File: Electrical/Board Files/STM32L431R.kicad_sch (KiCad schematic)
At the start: 11 parts, among them U3 STM32L431RCTx

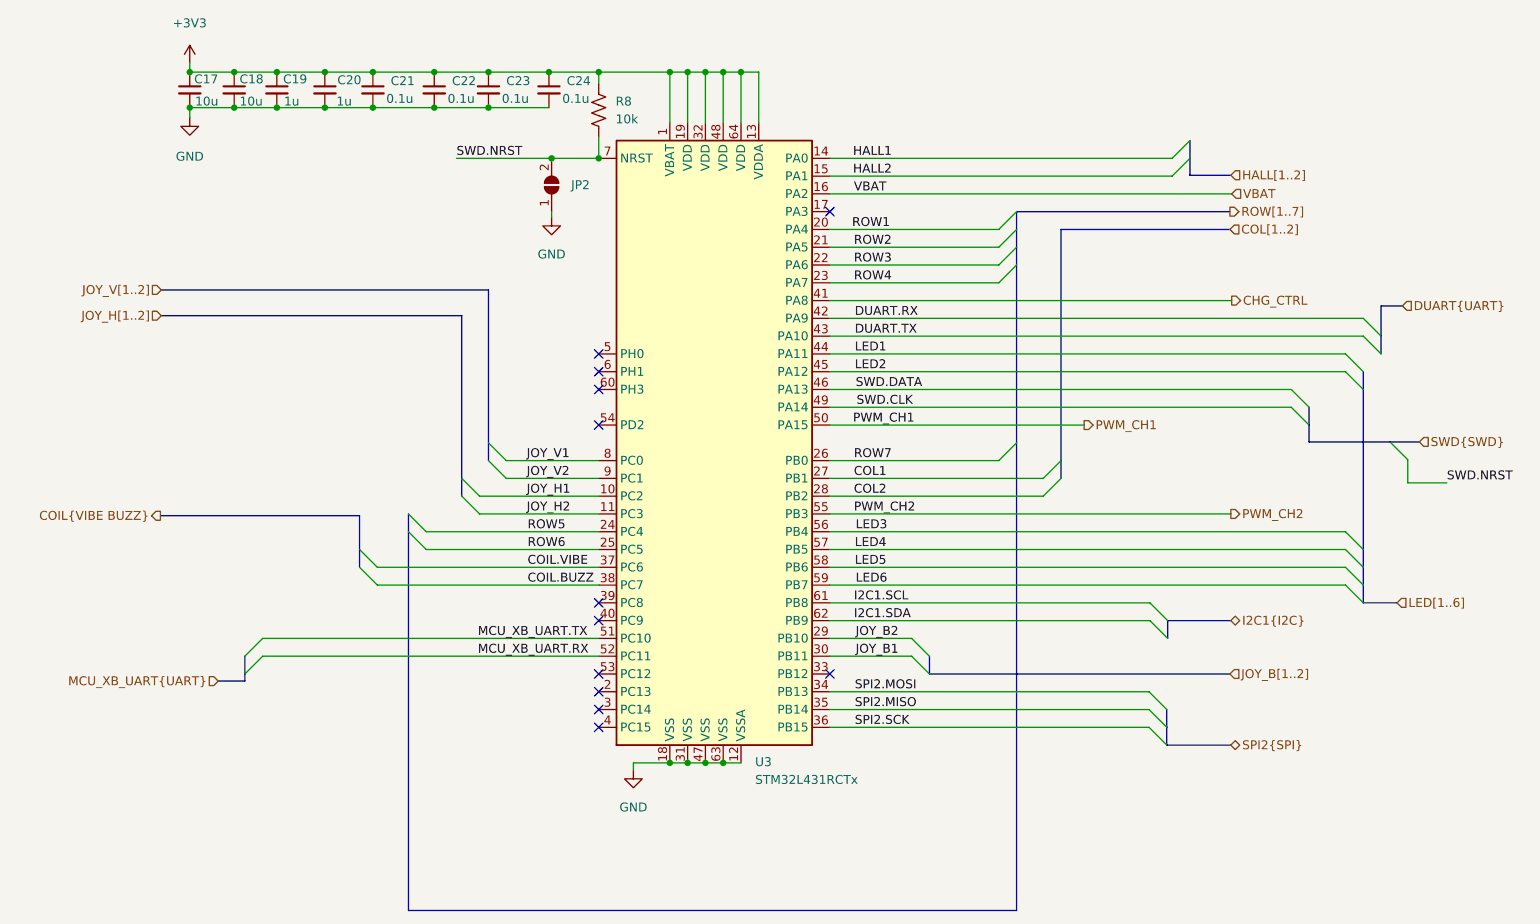
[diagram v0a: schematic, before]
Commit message: Fixing USB pins and added SPI_CS
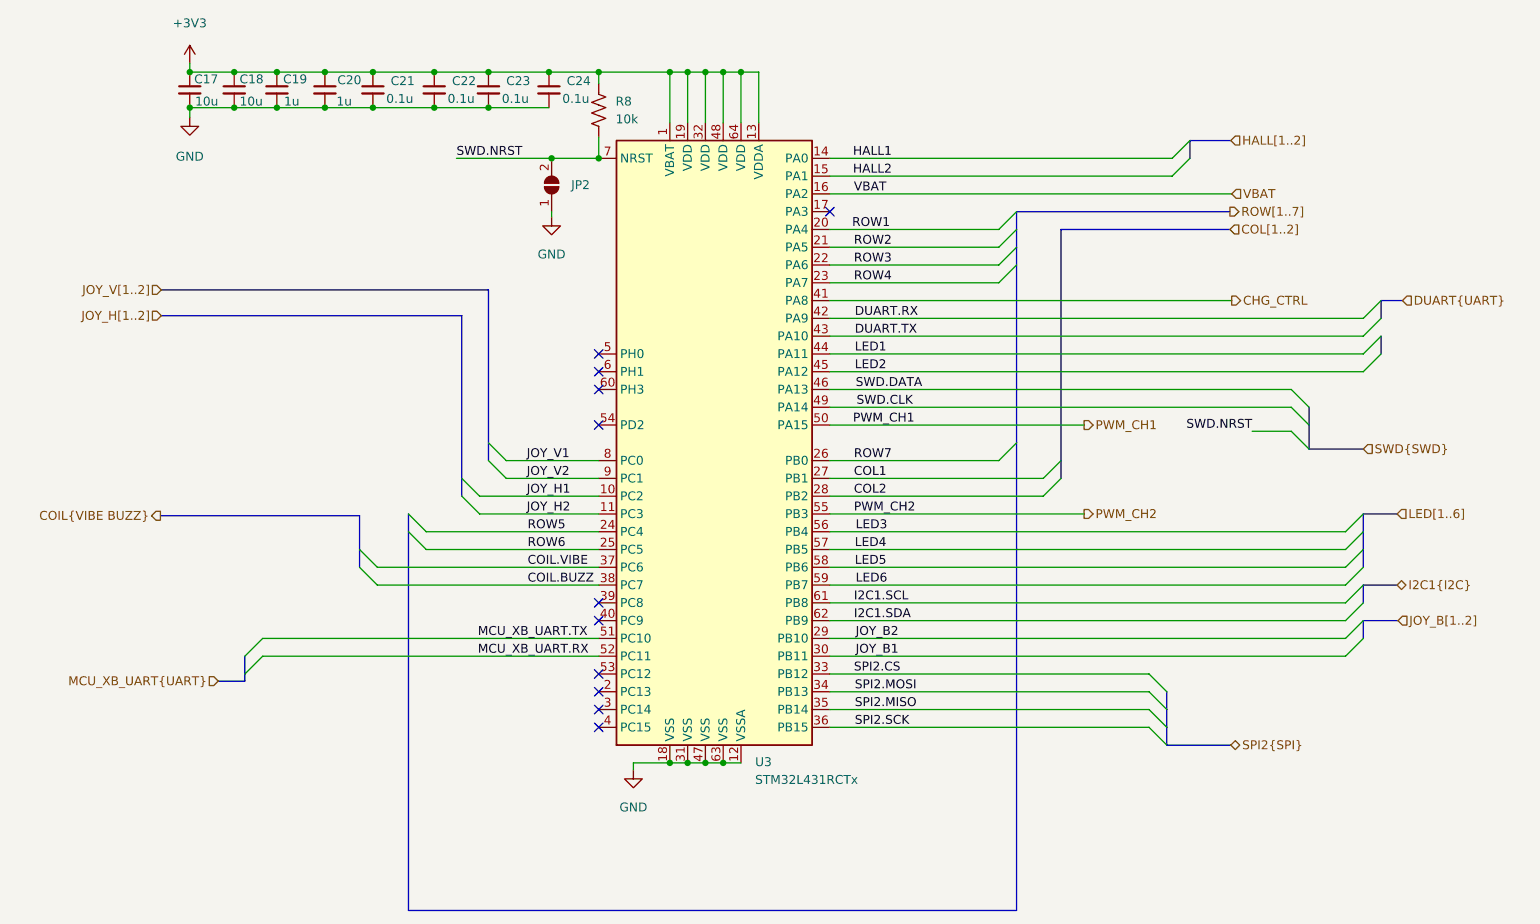
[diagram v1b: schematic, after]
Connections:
- net SPI2.CS: now reaches U3.33 (PB12)
- no-connect marks 12 -> 11

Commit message: Adding some device footprints and MPN
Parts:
- C17, C18: MANUFACTURER (none) -> CL10A106MA8NRNC
- C19, C20: MANUFACTURER (none) -> CL10A105KB8NNNC
- C21, C22, C23, C24: footprint (none) -> Capacitor_SMD:C_0603_1608Metric; MANUFACTURER (none) -> CC0603KRX7R9BB104
- JP2: footprint (none) -> Jumper:SolderJumper-3_P2.0mm_Open_TrianglePad1.0x1.5mm; MANUFACTURER (none) -> -
- R8: footprint (none) -> Resistor_SMD:R_0603_1608Metric
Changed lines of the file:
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@@
     (company "Rockerbotics")
   )
-  (bus_alias "SPI" (members "MOSI" "MISO" "SCK" "CS"))
-  (bus_alias "I2C" (members "SDA" "SCL"))
   (bus_alias "UART" (members "RX" "TX"))
   (bus_alias "SWD" (members "DATA" "CLK" "NRST"))
+  (bus_alias "I2C" (members "SDA" "SCL"))
+  (bus_alias "SPI" (members "MOSI" "MISO" "SCK" "CS"))
   (junction (at 109.982 44.323) (diameter 0) (color 0 0 0 0)
   )
@@
       (effects (font (size 1.27 1.27)) (justify left))
     )
-    (property "Footprint" "" (id 2) (at 126.746 44.958 90)
+    (property "Footprint" "Resistor_SMD:R_0603_1608Metric" (id 2) (at 126.746 44.958 90)
       (effects (font (size 1.27 1.27)) hide)
     )
@@
       (effects (font (size 1.27 1.27)) hide)
     )
+    (property "MANUFACTURER" "CL10A106MA8NRNC" (id 4) (at 67.31 41.783 0)
+      (effects (font (size 1.27 1.27)) hide)
+    )
     (pin "1")
     (pin "2")
@@
       (effects (font (size 1.27 1.27)) (justify left))
     )
-    (property "Footprint" "" (id 2) (at 93.472 41.783 0)
+    (property "Footprint" "Capacitor_SMD:C_0603_1608Metric" (id 2) (at 93.472 41.783 0)
       (effects (font (size 1.27 1.27)) hide)
     )
     (property "Datasheet" "~" (id 3) (at 93.472 41.783 0)
+      (effects (font (size 1.27 1.27)) hide)
+    )
+    (property "MANUFACTURER" "CC0603KRX7R9BB104" (id 4) (at 93.472 41.783 0)
       (effects (font (size 1.27 1.27)) hide)
     )
@@
       (effects (font (size 1.27 1.27)) (justify left))
     )
-    (property "Footprint" "" (id 2) (at 102.235 41.783 0)
+    (property "Footprint" "Capacitor_SMD:C_0603_1608Metric" (id 2) (at 102.235 41.783 0)
       (effects (font (size 1.27 1.27)) hide)
     )
     (property "Datasheet" "~" (id 3) (at 102.235 41.783 0)
+      (effects (font (size 1.27 1.27)) hide)
+    )
+    (property "MANUFACTURER" "CC0603KRX7R9BB104" (id 4) (at 102.235 41.783 0)
       (effects (font (size 1.27 1.27)) hide)
     )
@@
       (effects (font (size 1.27 1.27)) hide)
     )
+    (property "MANUFACTURER" "CL10A106MA8NRNC" (id 4) (at 73.66 41.783 0)
+      (effects (font (size 1.27 1.27)) hide)
+    )
     (pin "1")
     (pin "2")
@@
       (effects (font (size 1.27 1.27)) (justify left))
     )
-    (property "Footprint" "" (id 2) (at 109.982 41.783 0)
+    (property "Footprint" "Capacitor_SMD:C_0603_1608Metric" (id 2) (at 109.982 41.783 0)
       (effects (font (size 1.27 1.27)) hide)
     )
     (property "Datasheet" "~" (id 3) (at 109.982 41.783 0)
+      (effects (font (size 1.27 1.27)) hide)
+    )
+    (property "MANUFACTURER" "CC0603KRX7R9BB104" (id 4) (at 109.982 41.783 0)
       (effects (font (size 1.27 1.27)) hide)
     )
@@
       (effects (font (size 1.27 1.27)) hide)
     )
+    (property "MANUFACTURER" "CL10A105KB8NNNC" (id 4) (at 79.756 41.783 0)
+      (effects (font (size 1.27 1.27)) hide)
+    )
     (pin "1")
     (pin "2")
@@
       (effects (font (size 1.27 1.27)) (justify left))
     )
-    (property "Footprint" "" (id 2) (at 118.618 41.783 0)
+    (property "Footprint" "Capacitor_SMD:C_0603_1608Metric" (id 2) (at 118.618 41.783 0)
       (effects (font (size 1.27 1.27)) hide)
     )
     (property "Datasheet" "~" (id 3) (at 118.618 41.783 0)
+      (effects (font (size 1.27 1.27)) hide)
+    )
+    (property "MANUFACTURER" "CC0603KRX7R9BB104" (id 4) (at 118.618 41.783 0)
       (effects (font (size 1.27 1.27)) hide)
     )
@@
     )
     (property "Datasheet" "~" (id 3) (at 86.614 41.783 0)
+      (effects (font (size 1.27 1.27)) hide)
+    )
+    (property "MANUFACTURER" "CL10A105KB8NNNC" (id 4) (at 86.614 41.783 0)
       (effects (font (size 1.27 1.27)) hide)
     )
@@
       (effects (font (size 1.27 1.27)) (justify right) hide)
     )
-    (property "Footprint" "" (id 2) (at 118.999 55.372 0)
+    (property "Footprint" "Jumper:SolderJumper-3_P2.0mm_Open_TrianglePad1.0x1.5mm" (id 2) (at 118.999 55.372 0)
       (effects (font (size 1.27 1.27)) hide)
     )
@@
       (effects (font (size 1.27 1.27)) hide)
     )
+    (property "MANUFACTURER" "-" (id 4) (at 118.999 55.372 0)
+      (effects (font (size 1.27 1.27)) hide)
+    )

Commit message: Adding footprints
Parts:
- C17, C18, C19, C20: footprint (none) -> Capacitor_SMD:C_0805_2012Metric
- C21, C22, C23, C24: footprint Capacitor_SMD:C_0603_1608Metric -> Capacitor_SMD:C_0805_2012Metric
- renumbered R8 to R10
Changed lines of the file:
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@@
     (company "Rockerbotics")
   )
+  (bus_alias "SPI" (members "MOSI" "MISO" "SCK" "CS"))
+  (bus_alias "UART" (members "RX" "TX"))
+  (bus_alias "I2C" (members "SDA" "SCL"))
   (bus_alias "SWD" (members "DATA" "CLK" "NRST"))
-  (bus_alias "I2C" (members "SDA" "SCL"))
-  (bus_alias "UART" (members "RX" "TX"))
-  (bus_alias "SPI" (members "MOSI" "MISO" "SCK" "CS"))
   (junction (at 109.982 44.323) (diameter 0) (color 0 0 0 0)
   )
@@
   (symbol (lib_id "Device:R_US") (at 125.73 44.704 0) (unit 1)
     (in_bom yes) (on_board yes) (fields_autoplaced)
-    (property "Reference" "R8" (id 0) (at 128.143 43.4339 0)
+    (property "Reference" "R10" (id 0) (at 128.143 43.4339 0)
       (effects (font (size 1.27 1.27)) (justify left))
     )
@@
   (symbol (lib_id "power:GND") (at 130.683 138.938 0) (unit 1)
     (in_bom yes) (on_board yes) (fields_autoplaced)
-    (property "Reference" "#PWR017" (id 0) (at 130.683 145.288 0)
+    (property "Reference" "#PWR018" (id 0) (at 130.683 145.288 0)
       (effects (font (size 1.27 1.27)) hide)
     )
@@
       (effects (font (size 1.27 1.27)) (justify left))
     )
-    (property "Footprint" "" (id 2) (at 67.31 41.783 0)
+    (property "Footprint" "Capacitor_SMD:C_0805_2012Metric" (id 2) (at 67.31 41.783 0)
       (effects (font (size 1.27 1.27)) hide)
     )
@@
   (symbol (lib_id "power:GND") (at 118.999 59.944 0) (unit 1)
     (in_bom yes) (on_board yes) (fields_autoplaced)
-    (property "Reference" "#PWR016" (id 0) (at 118.999 66.294 0)
+    (property "Reference" "#PWR017" (id 0) (at 118.999 66.294 0)
       (effects (font (size 1.27 1.27)) hide)
     )
@@
       (effects (font (size 1.27 1.27)) (justify left))
     )
-    (property "Footprint" "Capacitor_SMD:C_0603_1608Metric" (id 2) (at 93.472 41.783 0)
+    (property "Footprint" "Capacitor_SMD:C_0805_2012Metric" (id 2) (at 93.472 41.783 0)
       (effects (font (size 1.27 1.27)) hide)
     )
@@
   (symbol (lib_id "power:GND") (at 67.31 45.72 0) (unit 1)
     (in_bom yes) (on_board yes) (fields_autoplaced)
-    (property "Reference" "#PWR015" (id 0) (at 67.31 52.07 0)
+    (property "Reference" "#PWR016" (id 0) (at 67.31 52.07 0)
       (effects (font (size 1.27 1.27)) hide)
     )
@@
       (effects (font (size 1.27 1.27)) (justify left))
     )
-    (property "Footprint" "Capacitor_SMD:C_0603_1608Metric" (id 2) (at 102.235 41.783 0)
+    (property "Footprint" "Capacitor_SMD:C_0805_2012Metric" (id 2) (at 102.235 41.783 0)
       (effects (font (size 1.27 1.27)) hide)
     )
@@
       (effects (font (size 1.27 1.27)) (justify left))
     )
-    (property "Footprint" "" (id 2) (at 73.66 41.783 0)
+    (property "Footprint" "Capacitor_SMD:C_0805_2012Metric" (id 2) (at 73.66 41.783 0)
       (effects (font (size 1.27 1.27)) hide)
     )
@@
       (effects (font (size 1.27 1.27)) (justify left))
     )
-    (property "Footprint" "Capacitor_SMD:C_0603_1608Metric" (id 2) (at 109.982 41.783 0)
+    (property "Footprint" "Capacitor_SMD:C_0805_2012Metric" (id 2) (at 109.982 41.783 0)
       (effects (font (size 1.27 1.27)) hide)
     )
@@
       (effects (font (size 1.27 1.27)) (justify left))
     )
-    (property "Footprint" "" (id 2) (at 79.756 41.783 0)
+    (property "Footprint" "Capacitor_SMD:C_0805_2012Metric" (id 2) (at 79.756 41.783 0)
       (effects (font (size 1.27 1.27)) hide)
     )
@@
       (effects (font (size 1.27 1.27)) (justify left))
     )
-    (property "Footprint" "Capacitor_SMD:C_0603_1608Metric" (id 2) (at 118.618 41.783 0)
+    (property "Footprint" "Capacitor_SMD:C_0805_2012Metric" (id 2) (at 118.618 41.783 0)
       (effects (font (size 1.27 1.27)) hide)
     )
@@
       (effects (font (size 1.27 1.27)) (justify left))
     )
-    (property "Footprint" "" (id 2) (at 86.614 41.783 0)
+    (property "Footprint" "Capacitor_SMD:C_0805_2012Metric" (id 2) (at 86.614 41.783 0)
       (effects (font (size 1.27 1.27)) hide)
     )
@@
   (symbol (lib_id "power:+3V3") (at 67.31 37.973 0) (unit 1)
     (in_bom yes) (on_board yes) (fields_autoplaced)
-    (property "Reference" "#PWR014" (id 0) (at 67.31 41.783 0)
-      (effects (font (size 1.27 1.27)) hide)
-    )
+    (property "Reference" "#PWR015" (id 0) (at 67.31 41.783 0)
+      (effects (font (size 1.27 1.27)) hide)
+    )
